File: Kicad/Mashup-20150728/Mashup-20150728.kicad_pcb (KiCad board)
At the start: 2 copper layers, 99.1 x 88.9 mm, 126 parts, among them P1 TST, P10 SPADE_187, P2 CONN_4, P3 CONN_4, P4 CONN2X3MOLEX, P4 CONN_4, P4 CONN_6, P4 SPADE_187, P5 CONN_4, P5 CONN_4X2, P5 CONN_8, P6 CONN_2, P6 CONN_4, P6 CONN_4X2, P6 CONN_8, P7 CONN_4, P7 CONN_8, Q1 MOSFET_N, Q2 MOSFET_N, Q3 MOSFET_N, Q4 MOSFET_N, Q5 MOSFET_N, Q6 MOSFET_N, Q7 MOSFET_N, Q8 MOSFET_N

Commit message: Added OPP logo to all boards.  Better late than never.
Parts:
- added VAL: REF, opp_logo_backsilk, F.Cu at (148.0, 114.9)
- added VAL: REF, opp_logo_backsilk, F.Cu at (202.6, 114.9)
- added VAL: REF, opp_logo_backsilk, F.Cu at (148.0, 140.3)
- added VAL: REF, opp_logo_backsilk, F.Cu at (193.0, 139.7)
- added VAL: REF, opp_logo_backsilk, F.Cu at (122.6, 155.6)
- added VAL: REF, opp_logo_backsilk, F.Cu at (177.2, 155.6)
- added VAL: REF, opp_logo_backsilk, F.Cu at (132.1, 180.3)
- added VAL: REF, opp_logo_backsilk, F.Cu at (187.3, 180.3)

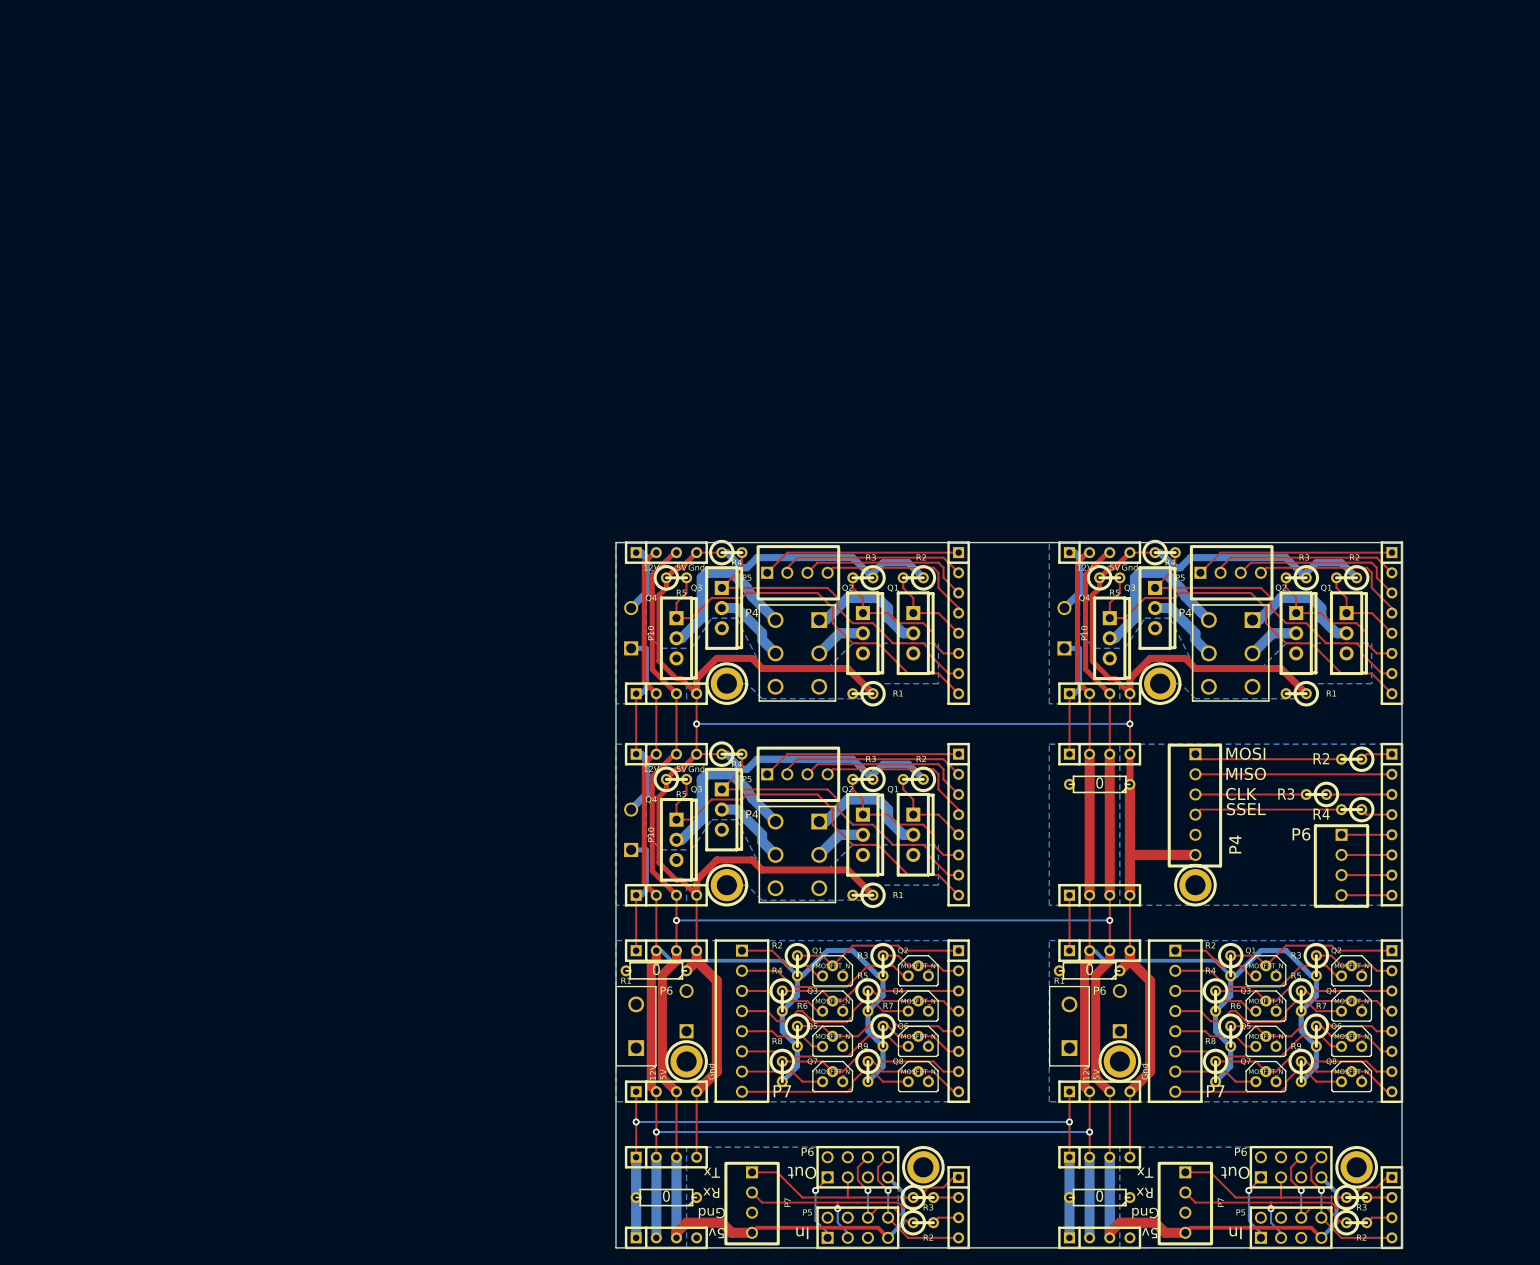
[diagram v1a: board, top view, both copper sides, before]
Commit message: Fix labeling issue on the incandescent board.
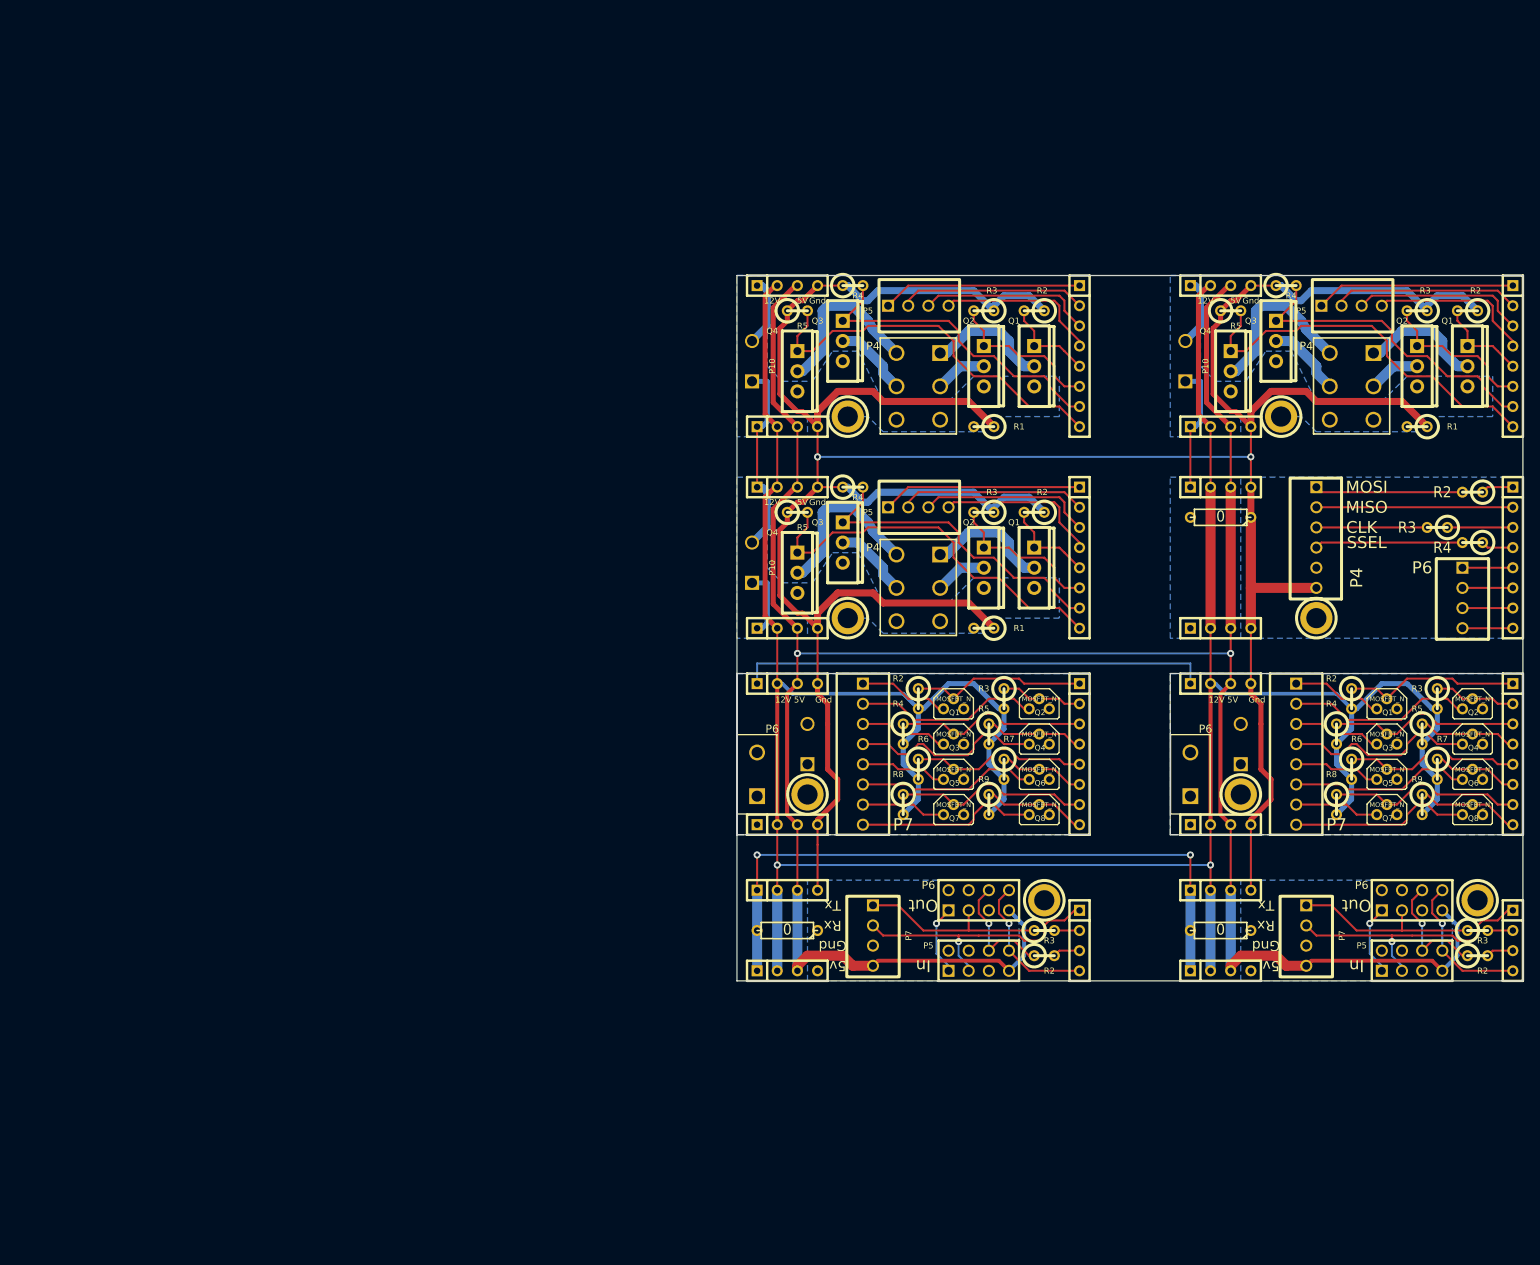
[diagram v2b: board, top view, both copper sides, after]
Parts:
- removed the P1 at (124.5, 140.3)
- removed the P1 at (119.4, 162.6)
- removed the P1 at (174.0, 162.6)
- removed the P1 at (179.1, 114.9)
- removed the P1 at (124.5, 114.9)
- removed the P1 at (203.8, 175.9)
- removed the P1 at (149.2, 175.9)
- removed the P10 at (167.0, 108.0)
- removed the P10 at (112.4, 133.3)
- removed the P10 at (112.4, 108.0)
- removed the P2 at (116.8, 148.6)
- removed the P2 at (171.4, 148.6)
- removed the P2 at (171.4, 98.4)
- removed the P2 at (116.8, 123.8)
- removed the P2 at (116.8, 98.4)
- removed the P2 at (171.4, 184.8)
- removed the P2 at (116.8, 184.8)
- removed the P3 at (116.8, 166.4)
- removed the P3 at (171.4, 166.4)
- removed the P3 at (171.4, 116.2)
- removed the P3 at (116.8, 141.6)
- removed the P3 at (116.8, 116.2)
- removed the P3 at (171.4, 174.6)
- removed the P3 at (116.8, 174.6)
- removed the P4 at (119.4, 156.2)
- removed the P4 at (174.0, 156.2)
- removed the P4 at (188.0, 111.1)
- removed the P4 at (133.3, 136.5)
- removed the P4 at (133.3, 111.1)
- removed the P4 at (208.3, 181.0)
- removed the P4 at (153.7, 181.0)
- removed the P5 at (153.7, 157.5)
- removed the P5 at (208.3, 157.5)
- removed the P5 at (188.0, 101.0)
- removed the P5 at (133.3, 126.4)
- removed the P5 at (133.3, 101.0)
- removed the P5 at (195.6, 183.5)
- removed the P5 at (141.0, 183.5)
- removed the P6 at (113.0, 158.1)
- removed the P6 at (167.6, 158.1)
- removed the P6 at (208.3, 107.3)
- removed the P6 at (153.7, 132.7)
- removed the P6 at (153.7, 107.3)
- removed the P6 at (195.6, 175.9)
- removed the P6 at (141.0, 175.9)
- removed the P7 at (126.4, 157.5)
- removed the P7 at (181.0, 157.5)
- removed the P7 at (182.2, 180.3)
- removed the P7 at (127.6, 180.3)
- removed the Q1 at (137.8, 151.1)
- removed the Q1 at (192.4, 151.1)
- removed the Q1 at (202.6, 108.6)
- removed the Q1 at (148.0, 134.0)
- removed the Q1 at (148.0, 108.6)
- removed the Q2 at (148.6, 151.1)
- removed the Q2 at (203.2, 151.1)
- removed the Q2 at (196.2, 108.6)
- removed the Q2 at (141.6, 134.0)
- removed the Q2 at (141.6, 108.6)
- removed the Q3 at (137.8, 155.6)
- removed the Q3 at (192.4, 155.6)
- removed the Q3 at (178.4, 105.4)
- removed the Q3 at (123.8, 130.8)
- removed the Q3 at (123.8, 105.4)
- removed the Q4 at (148.6, 155.6)
- removed the Q4 at (203.2, 155.6)
- removed the Q4 at (172.7, 109.2)
- removed the Q4 at (118.1, 134.6)
- removed the Q4 at (118.1, 109.2)
- removed the Q5 at (137.8, 160.0)
- removed the Q5 at (192.4, 160.0)
- removed the Q6 at (148.6, 160.0)
- removed the Q6 at (203.2, 160.0)
- removed the Q7 at (137.8, 164.5)
- removed the Q7 at (192.4, 164.5)
- removed the Q8 at (148.6, 164.5)
- removed the Q8 at (203.2, 164.5)
- removed the R1 at (115.6, 151.1)
- removed the R1 at (170.2, 151.1)
- removed the R1 at (196.2, 116.2)
- removed the R1 at (141.6, 141.6)
- removed the R1 at (141.6, 116.2)
- removed the R1 at (171.4, 179.7)
- removed the R1 at (116.8, 179.7)
- removed the R2 at (133.3, 150.5)
- removed the R2 at (188.0, 150.5)
- removed the R2 at (202.6, 101.6)
- removed the R2 at (148.0, 127.0)
- removed the R2 at (148.0, 101.6)
- removed the R2 at (203.8, 182.9)
- removed the R2 at (149.2, 182.9)
- removed the R3 at (144.1, 150.5)
- removed the R3 at (198.8, 150.5)
- removed the R3 at (196.2, 101.6)
- removed the R3 at (141.6, 127.0)
- removed the R3 at (141.6, 101.6)
- removed the R3 at (203.8, 179.7)
- removed the R3 at (149.2, 179.7)
- removed the R4 at (131.4, 154.9)
- removed the R4 at (186.1, 154.9)
- removed the R4 at (179.7, 98.4)
- removed the R4 at (125.1, 123.8)
- removed the R4 at (125.1, 98.4)
- removed the R5 at (142.2, 154.9)
- removed the R5 at (196.8, 154.9)
- removed the R5 at (172.7, 101.6)
- removed the R5 at (118.1, 127.0)
- removed the R5 at (118.1, 101.6)
- removed the R6 at (133.3, 159.4)
- removed the R6 at (188.0, 159.4)
- removed the R7 at (144.1, 159.4)
- removed the R7 at (198.8, 159.4)
- removed the R8 at (131.4, 163.8)
- removed the R8 at (186.1, 163.8)
- removed the R9 at (142.2, 163.8)
- removed the R9 at (196.8, 163.8)
- removed the VAL at (122.6, 155.6)
- removed the VAL at (177.2, 155.6)
- added P1: TST, 00_mtg_hole-2-56, F.Cu at (139.7, 106.7)
- added P1: TST, 00_mtg_hole-2-56, F.Cu at (194.3, 81.3)
- added P1: TST, 00_mtg_hole-2-56, F.Cu at (139.7, 81.3)
- added P1: TST, 00_mtg_hole-2-56, F.Cu at (219.1, 142.2)
- added P1: TST, 00_mtg_hole-2-56, F.Cu at (164.5, 142.2)
- added P1: TST, 00_mtg_hole-2-56, F.Cu at (134.6, 128.9)
- added P1: TST, 00_mtg_hole-2-56, F.Cu at (189.2, 128.9)
- added P10: SPADE_187, 00_th1x2x200, F.Cu at (182.2, 74.3)
- added P10: SPADE_187, 00_th1x2x200, F.Cu at (127.6, 99.7)
- added P10: SPADE_187, 00_th1x2x200, F.Cu at (127.6, 74.3)
- added P2: CONN_4, SIL-4, F.Cu at (186.7, 64.8)
- added P2: CONN_4, SIL-4, F.Cu at (132.1, 90.2)
- added P2: CONN_4, SIL-4, F.Cu at (132.1, 64.8)
- added P2: CONN_4, SIL-4, F.Cu at (186.7, 151.1)
- added P2: CONN_4, SIL-4, F.Cu at (132.1, 151.1)
- added P2: CONN_4, SIL-4, F.Cu at (132.1, 114.9)
- added P2: CONN_4, SIL-4, F.Cu at (186.7, 114.9)
- added P3: CONN_4, SIL-4, F.Cu at (186.7, 82.5)
- added P3: CONN_4, SIL-4, F.Cu at (132.1, 108.0)
- added P3: CONN_4, SIL-4, F.Cu at (132.1, 82.5)
- added P3: CONN_4, SIL-4, F.Cu at (186.7, 141.0)
- added P3: CONN_4, SIL-4, F.Cu at (132.1, 141.0)
- added P3: CONN_4, SIL-4, F.Cu at (132.1, 132.7)
- added P3: CONN_4, SIL-4, F.Cu at (186.7, 132.7)
- added P4: CONN2X3MOLEX, 00_th2x3x4.2mm_nopeg, F.Cu at (203.2, 77.5)
- added P4: CONN2X3MOLEX, 00_th2x3x4.2mm_nopeg, F.Cu at (148.6, 102.9)
- added P4: CONN2X3MOLEX, 00_th2x3x4.2mm_nopeg, F.Cu at (148.6, 77.5)
- added P4: CONN_4, SIL-4, F.Cu at (223.5, 147.3)
- added P4: CONN_4, SIL-4, F.Cu at (168.9, 147.3)
- added P4: SPADE_187, 00_th1x2x200, F.Cu at (134.6, 122.6)
- added P4: SPADE_187, 00_th1x2x200, F.Cu at (189.2, 122.6)
- added P5: CONN_4, 00_th1x4x100-lock, F.Cu at (203.2, 67.3)
- added P5: CONN_4, 00_th1x4x100-lock, F.Cu at (148.6, 92.7)
- added P5: CONN_4, 00_th1x4x100-lock, F.Cu at (148.6, 67.3)
- added P5: CONN_4X2, pin_array_4x2, F.Cu at (210.8, 149.9)
- added P5: CONN_4X2, pin_array_4x2, F.Cu at (156.2, 149.9)
- added P5: CONN_8, SIL-8, F.Cu at (168.9, 123.8)
- added P5: CONN_8, SIL-8, F.Cu at (223.5, 123.8)
- added P6: CONN_8, SIL-8, F.Cu at (223.5, 73.7)
- added P6: CONN_8, SIL-8, F.Cu at (168.9, 99.1)
- added P6: CONN_8, SIL-8, F.Cu at (168.9, 73.7)
- added P6: CONN_4X2, pin_array_4x2, F.Cu at (210.8, 142.2)
- added P6: CONN_4X2, pin_array_4x2, F.Cu at (156.2, 142.2)
- added P6: CONN_2, 00_th1x2x4.2mm_nopeg, F.Cu at (128.3, 126.4)
- added P6: CONN_2, 00_th1x2x4.2mm_nopeg, F.Cu at (182.9, 126.4)
- added P7: CONN_4, 00_th1x4x100-lock, F.Cu at (197.5, 146.7)
- added P7: CONN_4, 00_th1x4x100-lock, F.Cu at (142.9, 146.7)
- added P7: CONN_8, 00_th1x8x100-lock, F.Cu at (141.6, 123.8)
- added P7: CONN_8, 00_th1x8x100-lock, F.Cu at (196.2, 123.8)
- added Q1: MOSFET_N, 00_to220_vert_gds, F.Cu at (217.8, 74.9)
- added Q1: MOSFET_N, 00_to220_vert_gds, F.Cu at (163.2, 100.3)
- added Q1: MOSFET_N, 00_to220_vert_gds, F.Cu at (163.2, 74.9)
- added Q1: MOSFET_N, 00_to92_sgd, F.Cu at (153.0, 117.5)
- added Q1: MOSFET_N, 00_to92_sgd, F.Cu at (207.6, 117.5)
- added Q2: MOSFET_N, 00_to220_vert_gds, F.Cu at (211.5, 74.9)
- added Q2: MOSFET_N, 00_to220_vert_gds, F.Cu at (156.8, 100.3)
- added Q2: MOSFET_N, 00_to220_vert_gds, F.Cu at (156.8, 74.9)
- added Q2: MOSFET_N, 00_to92_sgd, F.Cu at (163.8, 117.5)
- added Q2: MOSFET_N, 00_to92_sgd, F.Cu at (218.4, 117.5)
- added Q3: MOSFET_N, 00_to220_vert_gds, F.Cu at (193.7, 71.8)
- added Q3: MOSFET_N, 00_to220_vert_gds, F.Cu at (139.1, 97.2)
- added Q3: MOSFET_N, 00_to220_vert_gds, F.Cu at (139.1, 71.8)
- added Q3: MOSFET_N, 00_to92_sgd, F.Cu at (153.0, 121.9)
- added Q3: MOSFET_N, 00_to92_sgd, F.Cu at (207.6, 121.9)
- added Q4: MOSFET_N, 00_to220_vert_gds, F.Cu at (188.0, 75.6)
- added Q4: MOSFET_N, 00_to220_vert_gds, F.Cu at (133.3, 101.0)
- added Q4: MOSFET_N, 00_to220_vert_gds, F.Cu at (133.3, 75.6)
- added Q4: MOSFET_N, 00_to92_sgd, F.Cu at (163.8, 121.9)
- added Q4: MOSFET_N, 00_to92_sgd, F.Cu at (218.4, 121.9)
- added Q5: MOSFET_N, 00_to92_sgd, F.Cu at (153.0, 126.4)
- added Q5: MOSFET_N, 00_to92_sgd, F.Cu at (207.6, 126.4)
- added Q6: MOSFET_N, 00_to92_sgd, F.Cu at (163.8, 126.4)
- added Q6: MOSFET_N, 00_to92_sgd, F.Cu at (218.4, 126.4)
- added Q7: MOSFET_N, 00_to92_sgd, F.Cu at (153.0, 130.8)
- added Q7: MOSFET_N, 00_to92_sgd, F.Cu at (207.6, 130.8)
- added Q8: MOSFET_N, 00_to92_sgd, F.Cu at (163.8, 130.8)
- added Q8: MOSFET_N, 00_to92_sgd, F.Cu at (218.4, 130.8)
- added R1: 100K, R1, F.Cu at (211.5, 82.5)
- added R1: 100K, R1, F.Cu at (156.8, 108.0)
- added R1: 100K, R1, F.Cu at (156.8, 82.5)
- added R1: 0, R3, F.Cu at (186.7, 146.1)
- added R1: 0, R3, F.Cu at (132.1, 146.1)
- added R2: 100K, R1, F.Cu at (217.8, 67.9)
- added R2: 100K, R1, F.Cu at (163.2, 93.3)
- added R2: 100K, R1, F.Cu at (163.2, 67.9)
- added R2: 480, R1, F.Cu at (219.1, 149.2)
- added R2: 480, R1, F.Cu at (164.5, 149.2)
- added R2: 10K, R1, F.Cu at (148.6, 116.8)
- added R2: 10K, R1, F.Cu at (203.2, 116.8)
- added R3: 100K, R1, F.Cu at (211.5, 67.9)
- added R3: 100K, R1, F.Cu at (156.8, 93.3)
- added R3: 100K, R1, F.Cu at (156.8, 67.9)
- added R3: 480, R1, F.Cu at (219.1, 146.1)
- added R3: 480, R1, F.Cu at (164.5, 146.1)
- added R3: 10K, R1, F.Cu at (159.4, 116.8)
- added R3: 10K, R1, F.Cu at (214.0, 116.8)
- added R4: 100K, R1, F.Cu at (194.9, 64.8)
- added R4: 100K, R1, F.Cu at (140.3, 90.2)
- added R4: 100K, R1, F.Cu at (140.3, 64.8)
- added R4: 10K, R1, F.Cu at (146.7, 121.3)
- added R4: 10K, R1, F.Cu at (201.3, 121.3)
- added R5: 0, R1, F.Cu at (188.0, 67.9)
- added R5: 0, R1, F.Cu at (133.3, 93.3)
- added R5: 0, R1, F.Cu at (133.3, 67.9)
- added R5: 10K, R1, F.Cu at (157.5, 121.3)
- added R5: 10K, R1, F.Cu at (212.1, 121.3)
- added R6: 10K, R1, F.Cu at (148.6, 125.7)
- added R6: 10K, R1, F.Cu at (203.2, 125.7)
- added R7: 10K, R1, F.Cu at (159.4, 125.7)
- added R7: 10K, R1, F.Cu at (214.0, 125.7)
- added R8: 10K, R1, F.Cu at (146.7, 130.2)
- added R8: 10K, R1, F.Cu at (201.3, 130.2)
- added R9: 10K, R1, F.Cu at (157.5, 130.2)
- added R9: 10K, R1, F.Cu at (212.1, 130.2)
- added VAL: REF, opp_logo_backsilk, F.Cu at (138.4, 122.6)
- added VAL: REF, opp_logo_backsilk, F.Cu at (193.0, 122.6)
- moved P4 36.9 mm to (198.8, 96.5)
- moved P1 36.9 mm to (198.8, 106.7)
- moved P3 36.9 mm to (186.7, 90.2)
- moved P5 36.9 mm to (223.5, 99.1)
- moved R1 36.9 mm to (186.7, 94.0)
- moved R3 36.9 mm to (214.0, 95.2)
- moved R4 36.9 mm to (218.4, 97.2)
- moved VAL 36.9 mm to (217.8, 81.3)
- moved VAL 36.9 mm to (202.6, 146.7)
- moved P2 36.9 mm to (186.7, 108.0)
- moved R2 36.9 mm to (218.4, 90.8)
- moved VAL 36.9 mm to (163.2, 81.3)
- moved VAL 36.9 mm to (163.2, 106.7)
- moved VAL 36.9 mm to (208.3, 106.0)
- moved VAL 36.9 mm to (147.3, 146.7)
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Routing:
- net +VLED: track 0.00 -> 59.7 mm
- net N-000007: track 0.00 -> 45.6 mm
- net N-000005: track 52.8 -> 80.6 mm
- net N-000002: track 49.2 -> 22.4 mm
- net N-000006: track 63.6 -> 39.7 mm
- net N-0000010: track 42.1 -> 19.7 mm
- net GNDPWR: track 172.2 -> 150.6 mm
- net GND: track 416.8 -> 413.3 mm
- net N-000008: track 87.5 -> 86.0 mm
- net N-000004: track 45.6 -> 46.9 mm
- net +12V1: track 360.5 -> 359.4 mm
- net N-000003: track 21.9 -> 23.0 mm
- net N-000009: track 142.0 -> 140.9 mm
- net +5V: track 315.0 -> 314.2 mm
- added copper zone on B.Cu, net +VLED
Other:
- outline, holes or cut-outs redrawn
